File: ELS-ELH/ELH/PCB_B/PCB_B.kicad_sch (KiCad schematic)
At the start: 24 parts, among them J1 Pressure Transducer Input, J11 Conn_01x09_Socket, J3 Conn_01x20_Pin, J4 Conn_01x20_Pin

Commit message: PCB B modified schematics
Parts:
- removed IMU1: MPU9250, ELH_Library:MPU9250, symbol ELH_Library:MPU9250
- removed J11: Conn_01x09_Socket, Connector_Hirose:Hirose_DF13-09P-1.25DSA_1x09_P1.25mm_Vertical, symbol Connector:Conn_01x09_Socket
- added U1: GY-87, ELH_Library:GY-87, symbol ELH_Library:GY-87
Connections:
- net GND1 is gone; now on net GND: GPS1.1 (GND)
- net PT_ADC2 is gone; now on net PT_ADC1: ADC1.4 (A0)
- net +3.3V: now also J4.13 (Pin_13), U1.2 (3.3V)
- net +5V: now also J4.14 (Pin_14)
- net GND: now also J3.1 (Pin_1), U1.3 (GND)
- net I2C1_SCL_1: now also U1.4 (SCL)
- net I2C1_SDA_1: now also U1.5 (SDA)
- net MOS1_2: now also J4.7 (Pin_7), J4.8 (Pin_8), J4.9 (Pin_9)
- net MOS2_2: now also J4.18 (Pin_18), J4.19 (Pin_19), J4.20 (Pin_20)
- net UART1_RX_2: now also J3.2 (Pin_2), J3.3 (Pin_3), J3.4 (Pin_4)
- net UART1_TX_2: now also J3.5 (Pin_5), J3.6 (Pin_6), J3.7 (Pin_7)
- net UART2_RX_1: now also ESP1.5 (D35)
- net UART2_RX_2: no longer ESP1.5 (D35)
- net UART2_TX_1: now also ESP1.9 (D26)
- net UART2_TX_2: no longer ESP1.9 (D26)
- no-connect marks 36 -> 35
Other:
- moved on the sheet: J3, J4

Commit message: PCB B connection advances
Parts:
- removed Bornera1: 5V Reg Output, ELH_Library:Bornera 2P, symbol Connector:Screw_Terminal_01x02
- removed GPS1: Ublox Neo-6m, ELH_Library:Ublox Neo-6m, symbol ELH_Library:Ublox_Neo-6m
- J1: footprint TerminalBlock:TerminalBlock_MaiXu_MX126-5.0-03P_1x03_P5.00mm -> ELH_Library:Bornera 3P
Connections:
- net CS_ALT: now also ESP1.28 (TX0); no longer ESP1.7 (D33)
- net CS_FLASH: now also ESP1.30 (D23); no longer ESP1.18 (D15)
- net GND: now also J3.20 (Pin_20), J4.12 (Pin_12); no longer ESP1.17 (GND), J3.1 (Pin_1)
- net I2C1_SCL: now also Converter1.13 (A2), U1.4 (SCL); no longer Converter1.12 (A1)
- net I2C1_SCL_1: now also Converter1.3 (B2); no longer Converter1.2 (B1), U1.4 (SCL)
- net I2C1_SDA: now also Converter1.12 (A1), U1.5 (SDA); no longer Converter1.13 (A2)
- net I2C1_SDA_1: now also Converter1.2 (B1); no longer Converter1.3 (B2), U1.5 (SDA)
- net LED1: now also Adapter1.12 (P7); no longer Adapter1.10 (P5)
- net LED3: now also Adapter1.10 (P5); no longer Adapter1.12 (P7)
- net PT_ADC1: now also ADC1.1 (A3); no longer ADC1.4 (A0)
- net SPI1_MOSI: now also ESP1.27 (RX0); no longer ESP1.30 (D23)
- net SPI2_MISO: now also ESP1.22 (D17); no longer ESP1.10 (D27)
- net SPI2_MOSI: now also ESP1.21 (D16); no longer ESP1.22 (D17)
- net SPI2_SCK: now also ESP1.23 (D5); no longer ESP1.21 (D16)
- net UART1_RX_2: now also J3.14 (Pin_14), J3.15 (Pin_15), J3.16 (Pin_16); no longer J3.2 (Pin_2), J3.3 (Pin_3), J3.4 (Pin_4)
- net UART1_TX_2: now also J3.17 (Pin_17), J3.18 (Pin_18), J3.19 (Pin_19); no longer J3.5 (Pin_5), J3.6 (Pin_6), J3.7 (Pin_7)
- net UART2_RX_1: now also Converter1.5 (B4); no longer Bornera7.2 (Pin_2), Converter1.4 (B3)
- net UART2_RX_2: now also Bornera7.2 (Pin_2), Converter1.15 (A4); no longer Converter1.14 (A3)
- net UART2_TX_1: now also Converter1.4 (B3); no longer Bornera7.1 (Pin_1), Converter1.5 (B4)
- net UART2_TX_2: now also Bornera7.1 (Pin_1), Converter1.14 (A3); no longer Converter1.15 (A4)
- net UART3_RX: now also J4.15 (Pin_15)
- net UART3_TX: now also J4.16 (Pin_16)
- net CS_IMURaw: no longer names the net of ESP1.20 (D4)
- no-connect marks 35 -> 37

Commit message: final updates
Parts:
- added J2: Conn_01x04_Pin, Connector_PinSocket_2.54mm:PinSocket_1x04_P2.54mm_Vertical, symbol Connector:Conn_01x04_Pin
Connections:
- net +3.3V: now also J3.5 (Pin_5), J3.6 (Pin_6), J3.7 (Pin_7), J4.11 (Pin_11), J4.12 (Pin_12), J2.4 (Pin_4)
- net +5V: now also J3.10 (Pin_10), J3.8 (Pin_8), J3.9 (Pin_9), J4.5 (Pin_5), J4.6 (Pin_6), J4.7 (Pin_7); no longer C13.1, C2.2, ESP1.15 (VIN), J4.14 (Pin_14)
- net GND: now also J3.14 (Pin_14), J3.15 (Pin_15), J3.16 (Pin_16), J4.17 (Pin_17), J4.2 (Pin_2), J4.3 (Pin_3), J4.4 (Pin_4), J2.1 (Pin_1); no longer J4.12 (Pin_12)
- net I2C1_SCL: now also Converter1.12 (A1); no longer Converter1.13 (A2)
- net I2C1_SCL_1: now also Converter1.2 (B1); no longer Converter1.3 (B2)
- net I2C1_SDA: now also Converter1.13 (A2); no longer Converter1.12 (A1)
- net I2C1_SDA_1: now also Converter1.3 (B2); no longer Converter1.2 (B1)
- net MOS1_2: now also J4.10 (Pin_10); no longer J4.7 (Pin_7)
- net UART1_RX_2: now also J3.11 (Pin_11), J3.12 (Pin_12), J3.13 (Pin_13); no longer J3.14 (Pin_14), J3.15 (Pin_15), J3.16 (Pin_16)
- net UART2_RX_1: now also Bornera7.2 (Pin_2); no longer ESP1.5 (D35)
- net UART2_RX_2: now also ESP1.5 (D35); no longer Bornera7.2 (Pin_2)
- net UART2_TX_1: now also Bornera7.1 (Pin_1); no longer ESP1.9 (D26)
- net UART2_TX_2: now also ESP1.9 (D26); no longer Bornera7.1 (Pin_1)
- net UART3_RX: now also J2.3 (Pin_3); no longer J4.15 (Pin_15)
- net UART3_TX: now also J2.2 (Pin_2); no longer J4.16 (Pin_16)
- net +5VA: now reaches J3.2 (Pin_2)
- net +5VA: now also C13.1, C2.2, ESP1.15 (VIN), J3.3 (Pin_3), J3.4 (Pin_4), J4.14 (Pin_14), J4.15 (Pin_15), J4.16 (Pin_16)

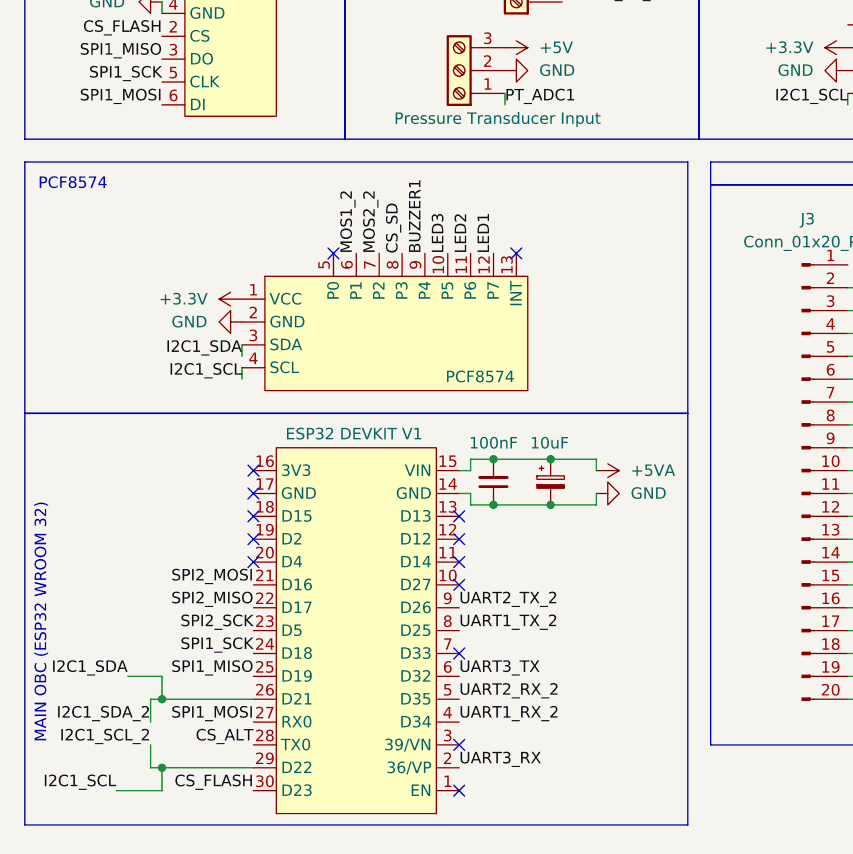
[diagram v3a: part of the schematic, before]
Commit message: PCB B reorganized
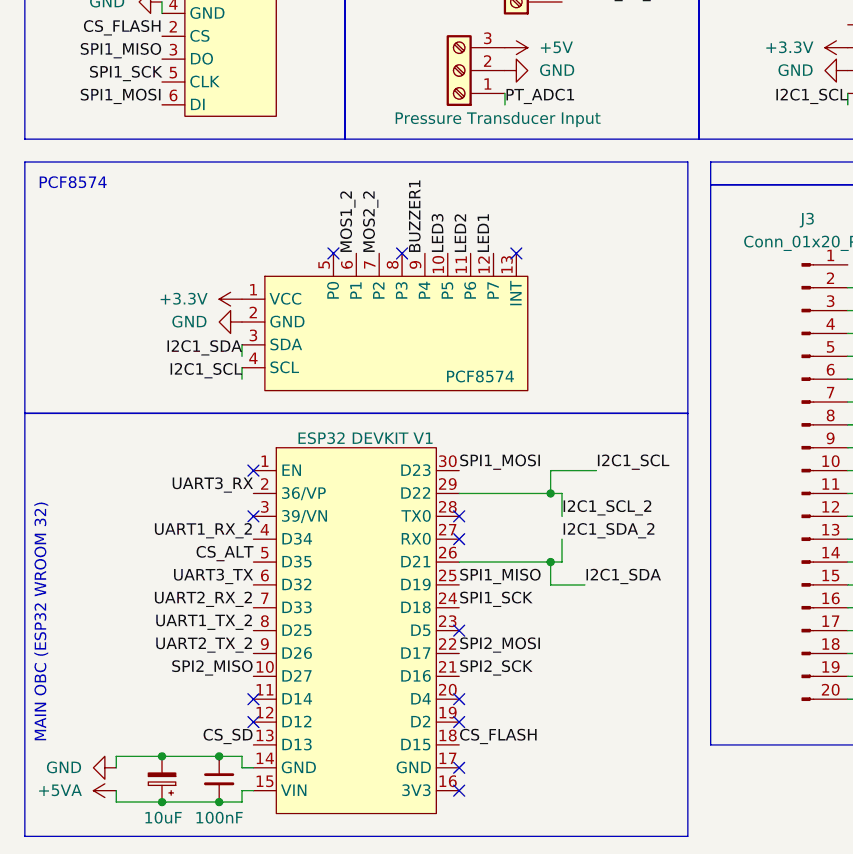
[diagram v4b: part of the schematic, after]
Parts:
- D10: footprint LED_THT:LED_D5.0mm-4_RGB_Staggered_Pins -> ELH_Library:LED RGB
- J3, J4: footprint Connector_PinSocket_2.54mm:PinSocket_1x20_P2.54mm_Vertical -> Connector_PinHeader_2.54mm:PinHeader_1x20_P2.54mm_Vertical
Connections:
- net CS_ALT: now also ESP1.5 (D35); no longer ESP1.28 (TX0)
- net CS_FLASH: now also ESP1.18 (D15); no longer ESP1.30 (D23)
- net CS_SD: now also ESP1.13 (D13); no longer Adapter1.8 (P3)
- net SPI1_MOSI: now also ESP1.30 (D23); no longer ESP1.27 (RX0)
- net SPI2_MISO: now also ESP1.10 (D27); no longer ESP1.22 (D17)
- net SPI2_MOSI: now also ESP1.22 (D17); no longer ESP1.21 (D16)
- net SPI2_SCK: now also ESP1.21 (D16); no longer ESP1.23 (D5)
- net UART2_RX_2: now also ESP1.7 (D33); no longer ESP1.5 (D35)

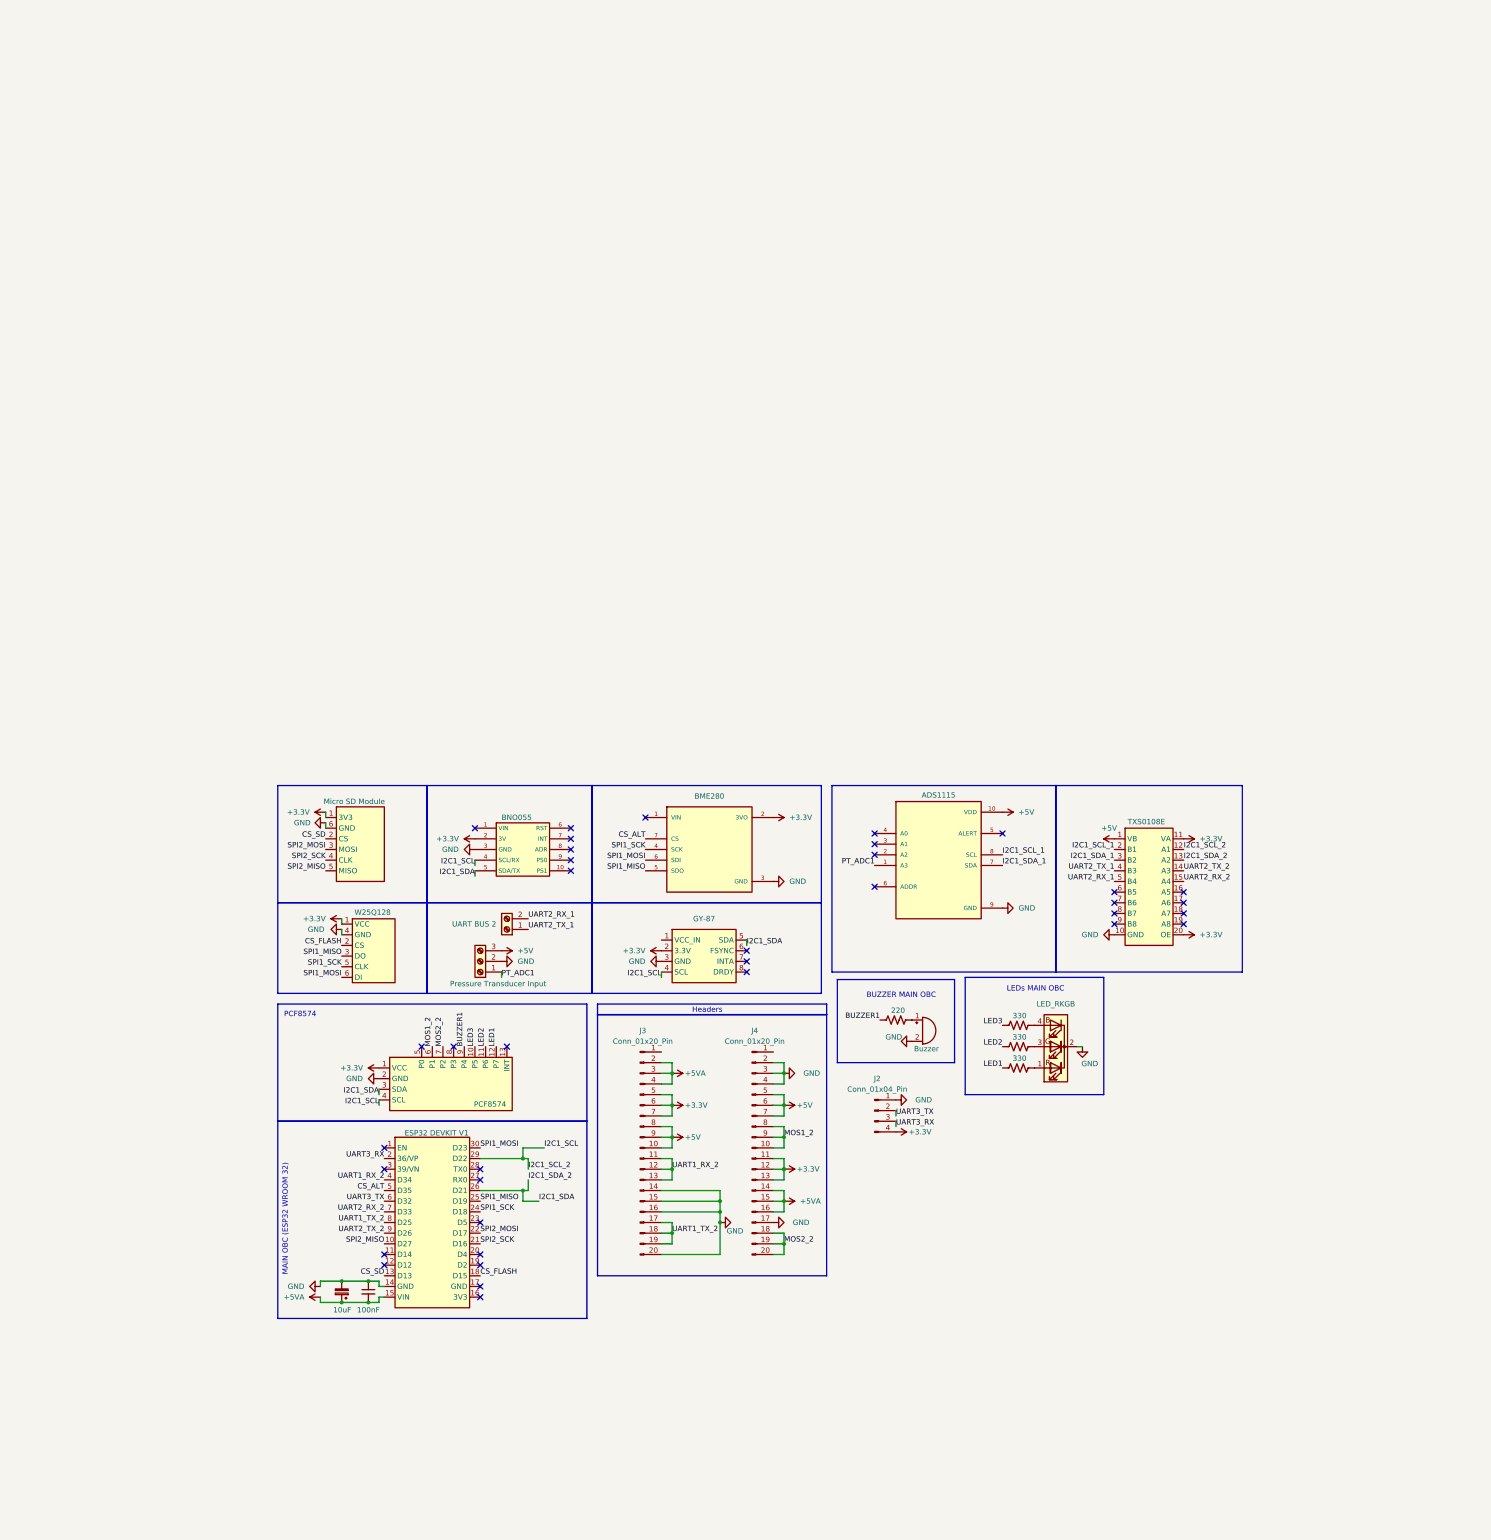
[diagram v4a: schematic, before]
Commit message: Update on net labels of both PCBs
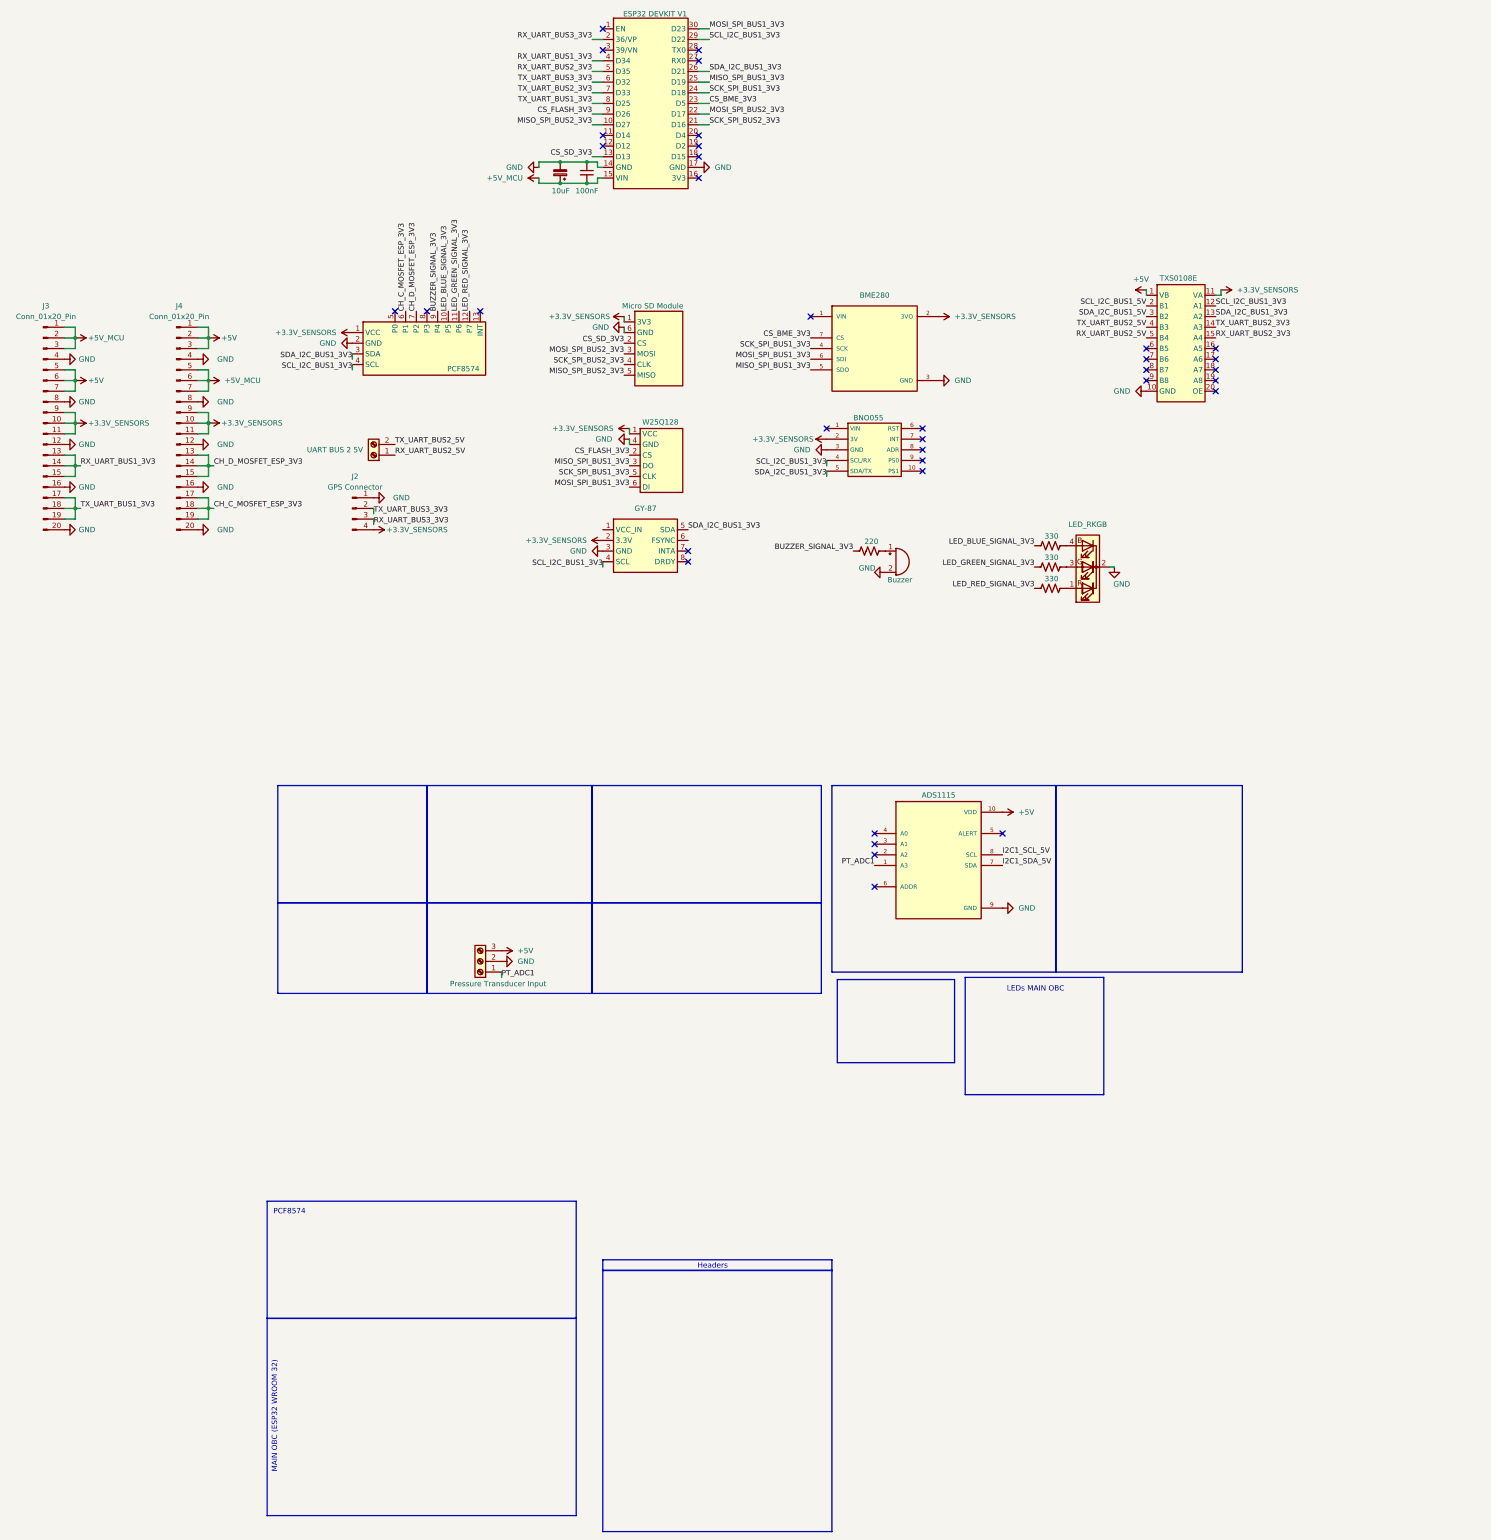
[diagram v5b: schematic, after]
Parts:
- Bornera7: value UART BUS 2 -> UART BUS 2 5V
- J2: value Conn_01x04_Pin -> GPS Connector
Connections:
- net +5V: now also J3.5 (Pin_5), J3.6 (Pin_6), J3.7 (Pin_7), J4.1 (Pin_1), J4.2 (Pin_2), J4.3 (Pin_3); no longer J3.10 (Pin_10), J3.8 (Pin_8), J3.9 (Pin_9), J4.5 (Pin_5), J4.6 (Pin_6), J4.7 (Pin_7)
- net GND: now also ESP1.17 (GND), J3.12 (Pin_12), J3.4 (Pin_4), J3.8 (Pin_8), J4.12 (Pin_12), J4.16 (Pin_16), J4.20 (Pin_20), J4.8 (Pin_8); no longer J3.14 (Pin_14), J3.15 (Pin_15), J4.17 (Pin_17), J4.2 (Pin_2), J4.3 (Pin_3)
- net CS_BME_3V3: now reaches ESP1.23 (D5)
- net CS_BME_3V3: now also BME2.7 (CS)
- net +5V_MCU: now reaches J3.1 (Pin_1)
- net +5V_MCU: now also C13.1, C2.2, ESP1.15 (VIN), J3.2 (Pin_2), J3.3 (Pin_3), J4.5 (Pin_5), J4.6 (Pin_6), J4.7 (Pin_7)
- net +3.3V renamed +3.3V_SENSORS
- net +3.3V_SENSORS: now also J3.10 (Pin_10), J3.11 (Pin_11), J3.9 (Pin_9), J4.10 (Pin_10), J4.9 (Pin_9); no longer Converter1.20 (OE), J3.5 (Pin_5), J3.6 (Pin_6), J3.7 (Pin_7), J4.12 (Pin_12), J4.13 (Pin_13)
- removed net +5VA: C13.1, C2.2, ESP1.15 (VIN), J3.2 (Pin_2), J3.3 (Pin_3), J3.4 (Pin_4), J4.14 (Pin_14), J4.15 (Pin_15), J4.16 (Pin_16)
- net BUZZER1 renamed BUZZER_SIGNAL_3V3
- net CS_ALT renamed RX_UART_BUS2_3V3
- net RX_UART_BUS2_3V3: now also Converter1.15 (A4); no longer BME2.7 (CS)
- net CS_FLASH: no longer names the net of ESP1.18 (D15)
- net CS_FLASH: no longer W25QXX1.2 (CS)
- net CS_SD renamed CS_SD_3V3
- net I2C1_SCL renamed SCL_I2C_BUS1_3V3
- net I2C1_SCL_1 renamed I2C1_SCL_5V
- net I2C1_SCL_5V: no longer Converter1.2 (B1)
- net I2C1_SDA renamed SDA_I2C_BUS1_3V3
- net I2C1_SDA_1 renamed I2C1_SDA_5V
- net I2C1_SDA_5V: no longer Converter1.3 (B2)
- net LED1 renamed LED_RED_SIGNAL_3V3
- net LED2 renamed LED_GREEN_SIGNAL_3V3
- net LED3 renamed LED_BLUE_SIGNAL_3V3
- removed net MOS1_2: Adapter1.6 (P1), J4.10 (Pin_10), J4.8 (Pin_8), J4.9 (Pin_9)
- net MOS2_2 renamed CH_C_MOSFET_ESP_3V3
- net CH_C_MOSFET_ESP_3V3: now also Adapter1.6 (P1), J4.17 (Pin_17); no longer Adapter1.7 (P2), J4.20 (Pin_20)
- net SPI1_MISO renamed MISO_SPI_BUS1_3V3
- net SPI1_MOSI renamed MOSI_SPI_BUS1_3V3
- net SPI1_SCK renamed SCK_SPI_BUS1_3V3
- net SPI2_MISO renamed MISO_SPI_BUS2_3V3
- net SPI2_MOSI renamed MOSI_SPI_BUS2_3V3
- net SPI2_SCK renamed SCK_SPI_BUS2_3V3
- net UART1_RX_2 renamed RX_UART_BUS1_3V3
- net RX_UART_BUS1_3V3: now also J3.14 (Pin_14), J3.15 (Pin_15); no longer J3.11 (Pin_11), J3.12 (Pin_12)
- net UART1_TX_2 renamed TX_UART_BUS1_3V3
- net UART2_RX_1 renamed RX_UART_BUS2_5V
- net RX_UART_BUS2_5V: now also Bornera7.1 (Pin_1); no longer Bornera7.2 (Pin_2)
- net UART2_RX_2 renamed TX_UART_BUS2_3V3
- net TX_UART_BUS2_3V3: now also Converter1.14 (A3); no longer Converter1.15 (A4)
- net UART2_TX_1 renamed TX_UART_BUS2_5V
- net TX_UART_BUS2_5V: now also Bornera7.2 (Pin_2); no longer Bornera7.1 (Pin_1)
- net UART2_TX_2 renamed CS_FLASH_3V3
- net CS_FLASH_3V3: now also W25QXX1.2 (CS); no longer Converter1.14 (A3)
- net UART3_RX renamed RX_UART_BUS3_3V3
- net UART3_TX renamed TX_UART_BUS3_3V3
- new net CH_D_MOSFET_ESP_3V3: Adapter1.7 (P2), J4.13 (Pin_13), J4.14 (Pin_14), J4.15 (Pin_15)
- new net SCL_I2C_BUS1_5V: Converter1.2 (B1)
- new net SDA_I2C_BUS1_5V: Converter1.3 (B2)
- no-connect marks 37 -> 36
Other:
- note removed: "BUZZER MAIN OBC"
